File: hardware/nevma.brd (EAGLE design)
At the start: 20 x 20 mm, 4 parts

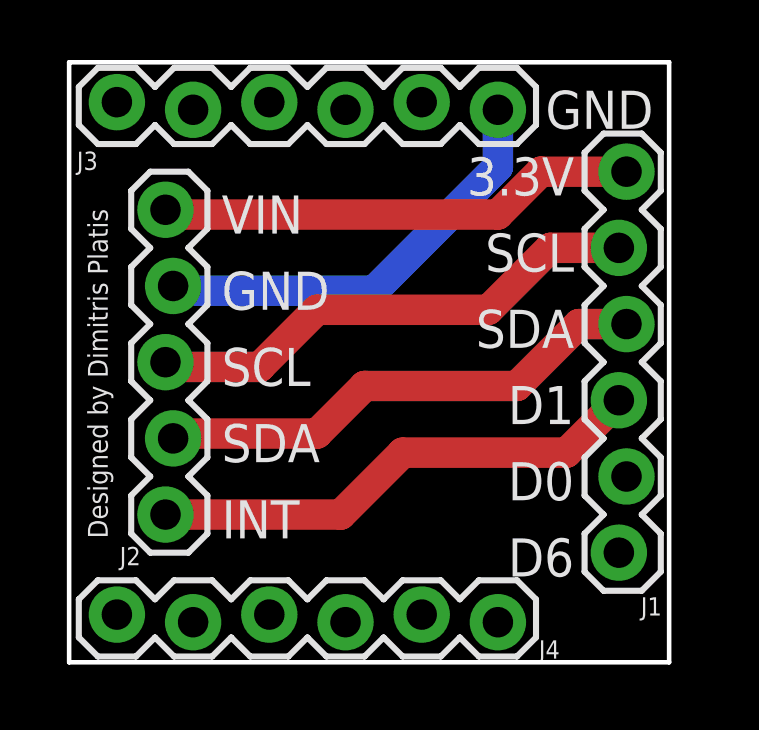
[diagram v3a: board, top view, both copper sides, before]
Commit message: Fix header position - HW rev. 2
* Also slightly decrease board size
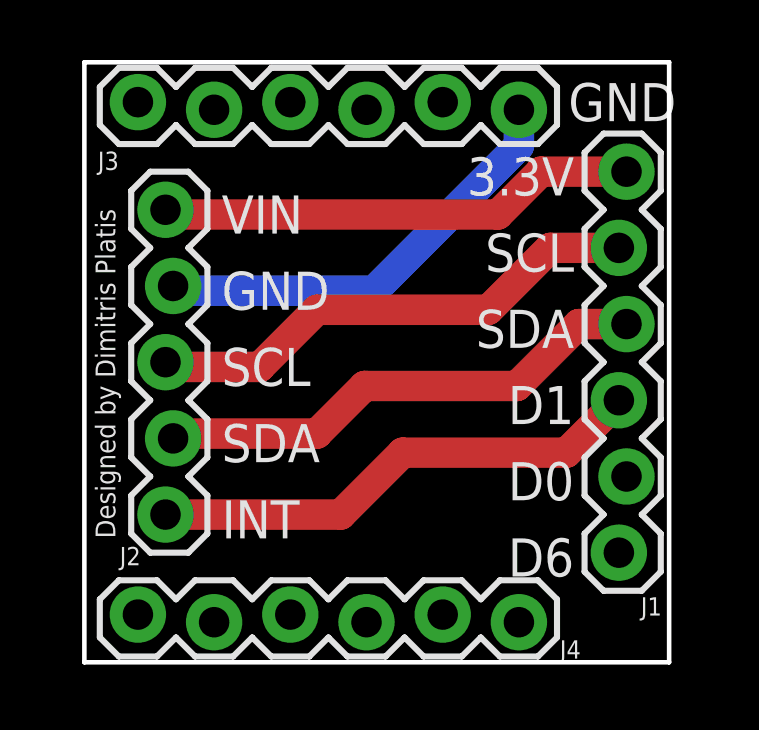
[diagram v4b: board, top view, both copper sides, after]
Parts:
- moved J3 0.70 mm to (55.0, 38.4)
- moved J4 0.70 mm to (55.0, 21.3)
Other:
- board size 20 x 20 mm -> 19.5 x 20 mm
- board text added: "Nevma board rev. 2"
- board text removed: "Nevma board rev. 1"
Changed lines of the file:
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@@
 <setting verticaltext="up"/>
 </settings>
-<grid distance="50" unitdist="mil" unit="mil" style="lines" multiple="1" display="yes" altdistance="5" altunitdist="mil" altunit="mil"/>
+<grid distance="10" unitdist="mil" unit="mil" style="lines" multiple="1" display="yes" altdistance="5" altunitdist="mil" altunit="mil"/>
 <layers>
 <layer number="1" name="Top" color="4" fill="1" visible="yes" active="yes"/>
@@
 <plain>
 <text x="48.51783125" y="27.86815625" size="1.9304" layer="22" font="vector" ratio="18" distance="10" rot="MR230" align="top-center">Nevma board
-rev. 1</text>
-<wire x1="40" y1="40" x2="60" y2="40" width="0.1524" layer="20"/>
-<wire x1="40" y1="20" x2="40" y2="40" width="0.1524" layer="20"/>
-<wire x1="60" y1="20" x2="40" y2="20" width="0.1524" layer="20"/>
+rev. 2</text>
+<wire x1="40.508" y1="40" x2="60" y2="40" width="0.1524" layer="20"/>
+<wire x1="40.508" y1="20" x2="40.508" y2="40" width="0.1524" layer="20"/>
+<wire x1="60" y1="20" x2="40.508" y2="20" width="0.1524" layer="20"/>
 <wire x1="60" y1="40" x2="60" y2="20" width="0.1524" layer="20"/>
 <text x="56.8325" y="29.845" size="1.27" layer="21" font="vector" ratio="10" distance="100" align="center-right">3.3V
@@
 SDA
 INT</text>
-<text x="55.88" y="38.4175" size="1.27" layer="21" font="vector" ratio="10" distance="100" align="center-left">GND</text>
-<text x="40.9575" y="24.13" size="0.6604" layer="21" font="vector" ratio="10" distance="100" rot="R90" align="center-left">Designed by Dimitris Platis</text>
+<text x="56.642" y="38.6715" size="1.27" layer="21" font="vector" ratio="10" distance="100" align="center-left">GND</text>
+<text x="41.2115" y="24.13" size="0.6604" layer="21" font="vector" ratio="10" distance="100" rot="R90" align="center-left">Designed by Dimitris Platis</text>
 </plain>
 <attributes>
@@
 <attribute name="VALUE" x="56.29275" y="37.62375" size="0.6096" layer="27" font="vector" ratio="20" rot="R270"/>
 </element>
-<element name="J3" library="SparkFun-Connectors" library_urn="urn:adsk.eagle:library:513" package="1X06_LOCK" package3d_urn="urn:adsk.eagle:package:38002/1" value="" x="54.2925" y="38.4175" smashed="yes" rot="R180">
-<attribute name="NAME" x="40.9575" y="37.0205" size="0.6096" layer="25" font="vector" ratio="20" rot="R180"/>
-<attribute name="VALUE" x="55.5625" y="40.7035" size="0.6096" layer="27" font="vector" ratio="20" rot="R180"/>
+<element name="J3" library="SparkFun-Connectors" library_urn="urn:adsk.eagle:library:513" package="1X06_LOCK" package3d_urn="urn:adsk.eagle:package:38002/1" value="" x="54.9925" y="38.4175" smashed="yes" rot="R180">
+<attribute name="NAME" x="41.6575" y="37.0205" size="0.6096" layer="25" font="vector" ratio="20" rot="R180"/>
+<attribute name="VALUE" x="56.2625" y="40.7035" size="0.6096" layer="27" font="vector" ratio="20" rot="R180"/>
 </element>
-<element name="J4" library="SparkFun-Connectors" library_urn="urn:adsk.eagle:library:513" package="1X06_LOCK" package3d_urn="urn:adsk.eagle:package:38002/1" value="" x="54.2925" y="21.336" smashed="yes" rot="R180">
-<attribute name="NAME" x="56.35625" y="20.73275" size="0.6096" layer="25" font="vector" ratio="20" rot="R180"/>
-<attribute name="VALUE" x="55.5625" y="23.622" size="0.6096" layer="27" font="vector" ratio="20" rot="R180"/>
+<element name="J4" library="SparkFun-Connectors" library_urn="urn:adsk.eagle:library:513" package="1X06_LOCK" package3d_urn="urn:adsk.eagle:package:38002/1" value="" x="54.9925" y="21.336" smashed="yes" rot="R180">
+<attribute name="NAME" x="57.05625" y="20.73275" size="0.6096" layer="25" font="vector" ratio="20" rot="R180"/>
+<attribute name="VALUE" x="56.2625" y="23.622" size="0.6096" layer="27" font="vector" ratio="20" rot="R180"/>
 </element>
 </elements>
@@
 <contactref element="J2" pad="4"/>
 <contactref element="J3" pad="1"/>
-<wire x1="54.2925" y1="38.4175" x2="54.2925" y2="36.5125" width="1.016" layer="16"/>
-<wire x1="54.2925" y1="36.5125" x2="50.165" y2="32.385" width="1.016" layer="16"/>
-<wire x1="50.165" y1="32.385" x2="43.6245" y2="32.385" width="1.016" layer="16"/>
+<wire x1="43.6245" y1="32.385" x2="50.165" y2="32.385" width="1.016" layer="16"/>
 <wire x1="43.6245" y1="32.385" x2="43.46575" y2="32.54375" width="1.016" layer="16"/>
 <polygon width="0.254" layer="16">
-<vertex x="40.005" y="40.005"/>
+<vertex x="40.513" y="40.005"/>
 <vertex x="60.0075" y="40.005"/>
-<vertex x="60.0075" y="20.32"/>
 <vertex x="60.0075" y="20.0025"/>
-<vertex x="40.005" y="20.0025"/>
+<vertex x="40.513" y="20.0025"/>
 </polygon>
+<wire x1="54.9925" y1="37.2125" x2="54.9925" y2="38.4175" width="1.016" layer="16"/>
+<wire x1="50.165" y1="32.385" x2="54.9925" y2="37.2125" width="1.016" layer="16"/>
 </signal>
 <signal name="SDA">

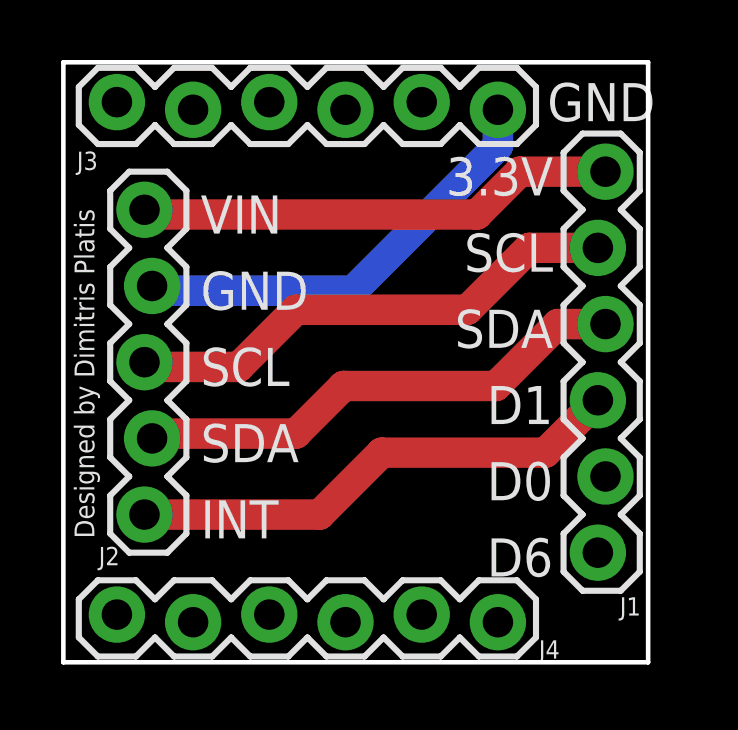
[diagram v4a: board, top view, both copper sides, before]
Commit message: Decrease board size further
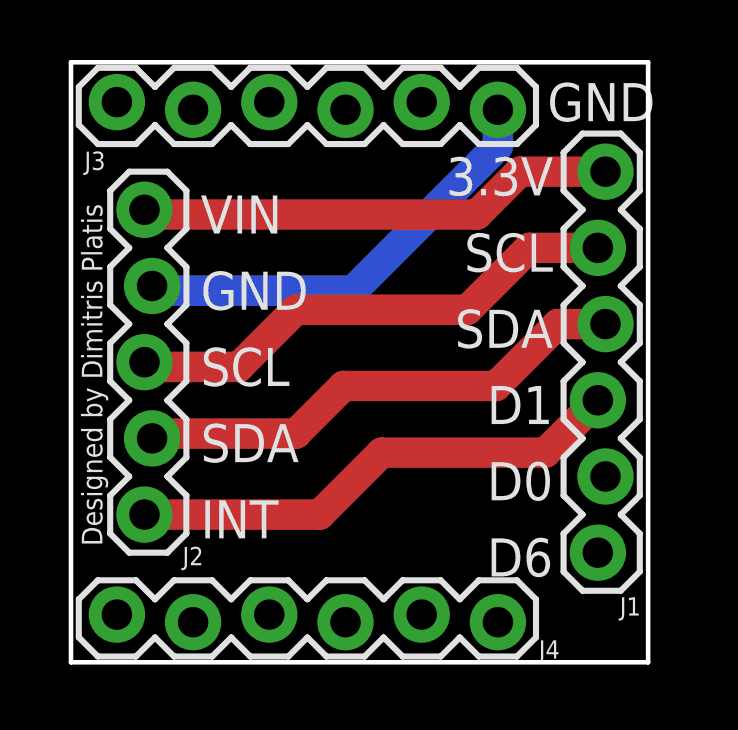
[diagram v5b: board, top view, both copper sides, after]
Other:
- board size 19.5 x 20 mm -> 19.2 x 20 mm
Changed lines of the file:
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@@
 <text x="48.51783125" y="27.86815625" size="1.9304" layer="22" font="vector" ratio="18" distance="10" rot="MR230" align="top-center">Nevma board
 rev. 2</text>
-<wire x1="40.508" y1="40" x2="60" y2="40" width="0.1524" layer="20"/>
-<wire x1="40.508" y1="20" x2="40.508" y2="40" width="0.1524" layer="20"/>
-<wire x1="60" y1="20" x2="40.508" y2="20" width="0.1524" layer="20"/>
+<wire x1="40.762" y1="40" x2="60" y2="40" width="0.1524" layer="20"/>
+<wire x1="40.762" y1="20" x2="40.762" y2="40" width="0.1524" layer="20"/>
+<wire x1="60" y1="20" x2="40.762" y2="20" width="0.1524" layer="20"/>
 <wire x1="60" y1="40" x2="60" y2="20" width="0.1524" layer="20"/>
 <text x="56.8325" y="29.845" size="1.27" layer="21" font="vector" ratio="10" distance="100" align="center-right">3.3V
@@
 INT</text>
 <text x="56.642" y="38.6715" size="1.27" layer="21" font="vector" ratio="10" distance="100" align="center-left">GND</text>
-<text x="41.2115" y="24.13" size="0.6604" layer="21" font="vector" ratio="10" distance="100" rot="R90" align="center-left">Designed by Dimitris Platis</text>
+<text x="41.4655" y="23.876" size="0.6858" layer="21" font="vector" ratio="10" distance="100" rot="R90" align="center-left">Designed by Dimitris Platis</text>
 </plain>
 <attributes>
@@
 <elements>
 <element name="J2" library="SparkFun-Connectors" library_urn="urn:adsk.eagle:library:513" package="1X05_LOCK" package3d_urn="urn:adsk.eagle:package:38105/1" value="" x="43.33875" y="24.92375" smashed="yes" rot="R90">
-<attribute name="NAME" x="42.38625" y="23.84425" size="0.6096" layer="25" font="vector" ratio="20" rot="R180"/>
+<attribute name="NAME" x="45.18025" y="23.84425" size="0.6096" layer="25" font="vector" ratio="20" rot="R180"/>
 <attribute name="VALUE" x="45.37075" y="23.65375" size="0.6096" layer="27" font="vector" ratio="20" rot="R90"/>
 </element>
@@
 </element>
 <element name="J3" library="SparkFun-Connectors" library_urn="urn:adsk.eagle:library:513" package="1X06_LOCK" package3d_urn="urn:adsk.eagle:package:38002/1" value="" x="54.9925" y="38.4175" smashed="yes" rot="R180">
-<attribute name="NAME" x="41.6575" y="37.0205" size="0.6096" layer="25" font="vector" ratio="20" rot="R180"/>
+<attribute name="NAME" x="41.9115" y="37.0205" size="0.6096" layer="25" font="vector" ratio="20" rot="R180"/>
 <attribute name="VALUE" x="56.2625" y="40.7035" size="0.6096" layer="27" font="vector" ratio="20" rot="R180"/>
 </element>
@@
 <wire x1="43.6245" y1="32.385" x2="43.46575" y2="32.54375" width="1.016" layer="16"/>
 <polygon width="0.254" layer="16">
-<vertex x="40.513" y="40.005"/>
+<vertex x="40.767" y="40.005"/>
 <vertex x="60.0075" y="40.005"/>
 <vertex x="60.0075" y="20.0025"/>
-<vertex x="40.513" y="20.0025"/>
+<vertex x="40.767" y="20.0025"/>
 </polygon>
 <wire x1="54.9925" y1="37.2125" x2="54.9925" y2="38.4175" width="1.016" layer="16"/>
